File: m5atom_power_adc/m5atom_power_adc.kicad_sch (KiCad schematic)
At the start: 45 parts, among them J1 USB_C_Receptacle_USB2.0_14P, U1 LM2596S-5, U2 ESP32-S3-MINI-1, U3 AMS1117-3.3, U4 ADS1115IDGS, U5 AMS1117-3.3

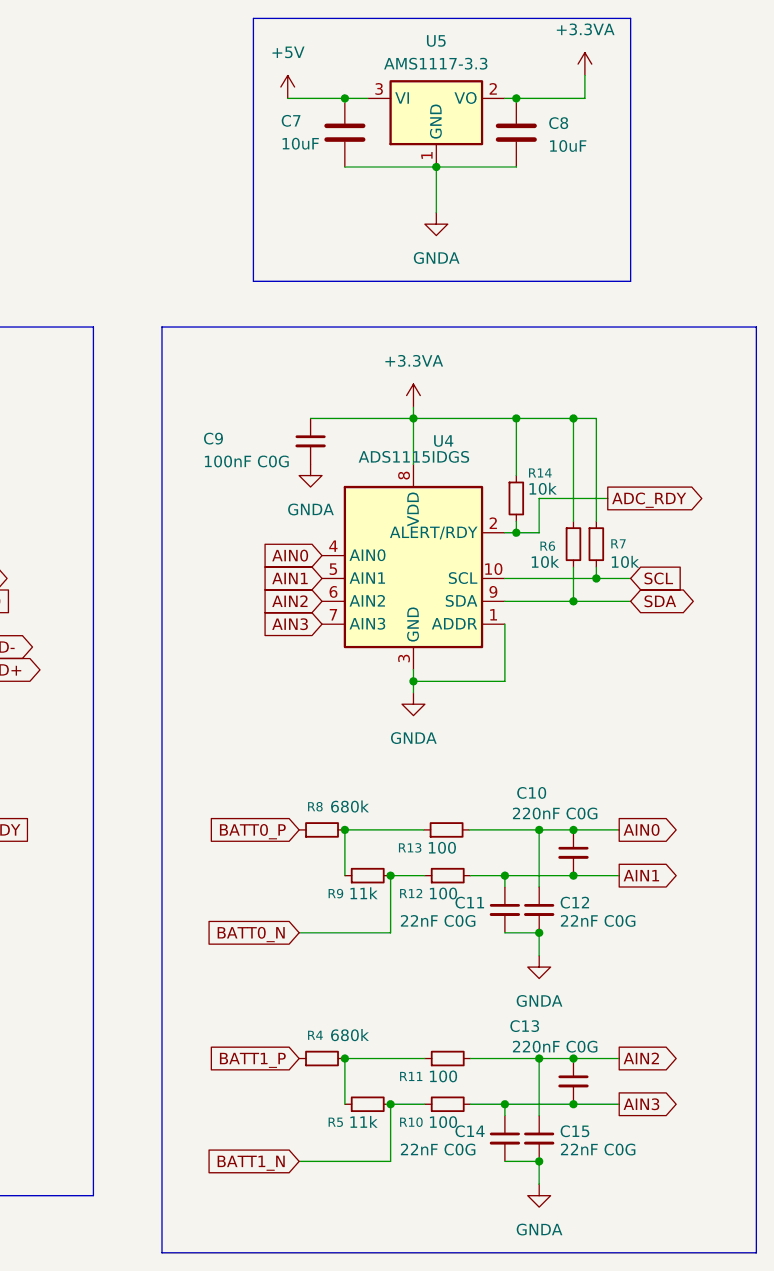
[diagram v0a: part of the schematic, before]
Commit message: chore: ADC周辺回路の修正（フェライトビーズ追加・分圧抵抗変更）
- FB1（フェライトビーズ 600Ω@100MHz）を5V→AMS1117間に追加
- C16（100nF）をフェライトビーズ前段に追加
- C7を10uF→47uFに増量
- R9・R5を11k→22kに変更（ADC分圧比改善）

Co-Authored-By: Claude Sonnet 4.6 <noreply@anthropic.com>
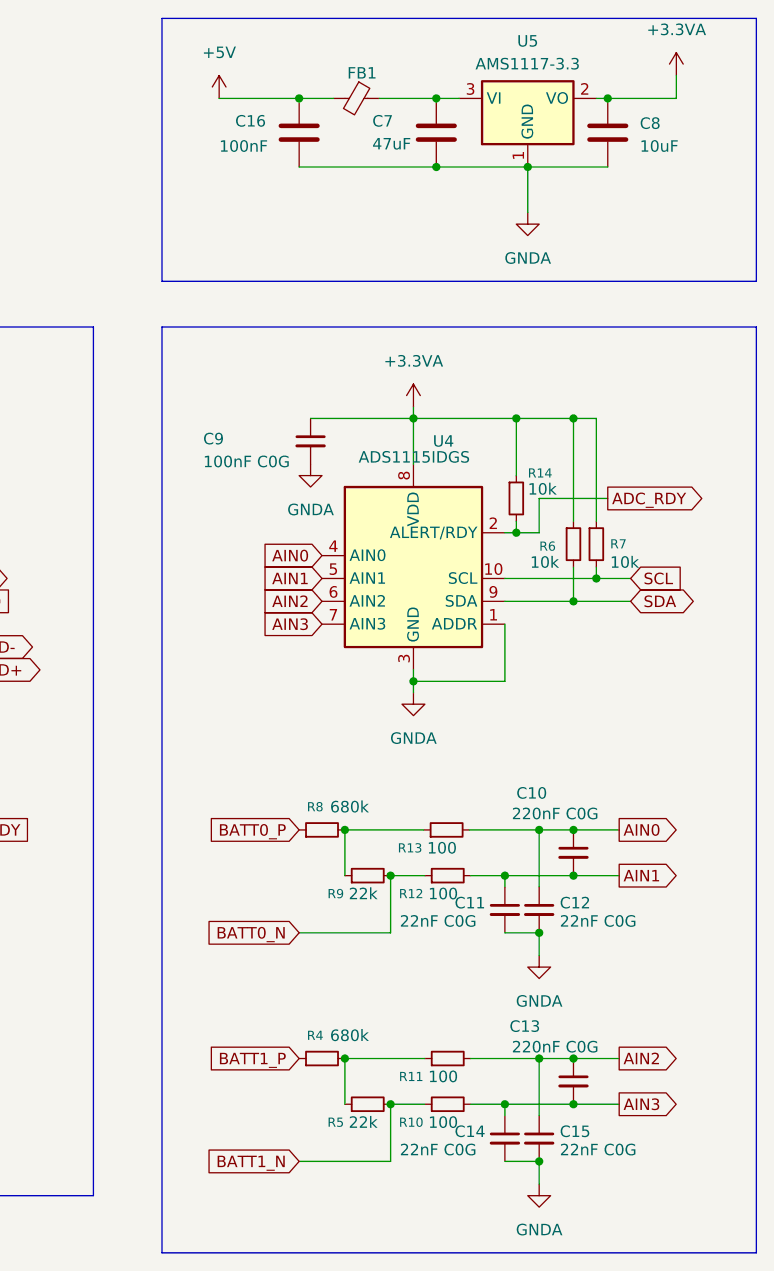
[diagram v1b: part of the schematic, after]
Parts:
- added C16: 100nF, symbol Device:C
- added FB1: 500mA 600Ω@100MHz, symbol Device:FerriteBead_Small
- C7: value 10uF -> 47uF
- R5, R9: value 11k -> 22k
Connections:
- net +5V: now also C16.1, FB1.2; no longer C7.1, U5.3 (VI)
- net GNDA: now also C16.2
- new net: C7.1, FB1.1, U5.3 (VI)
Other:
- moved on the sheet: C7, C8, U5
